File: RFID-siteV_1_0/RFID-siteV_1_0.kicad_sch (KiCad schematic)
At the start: 48 parts, among them J1 USB_C_Receptacle_USB2.0, J2 Conn_01x05_Male, J4 Conn_01x05_Female, Q1 MMBT3904, SW1 SW_Push, U1 XC6206P332MR, U2 STM32L053R8Tx

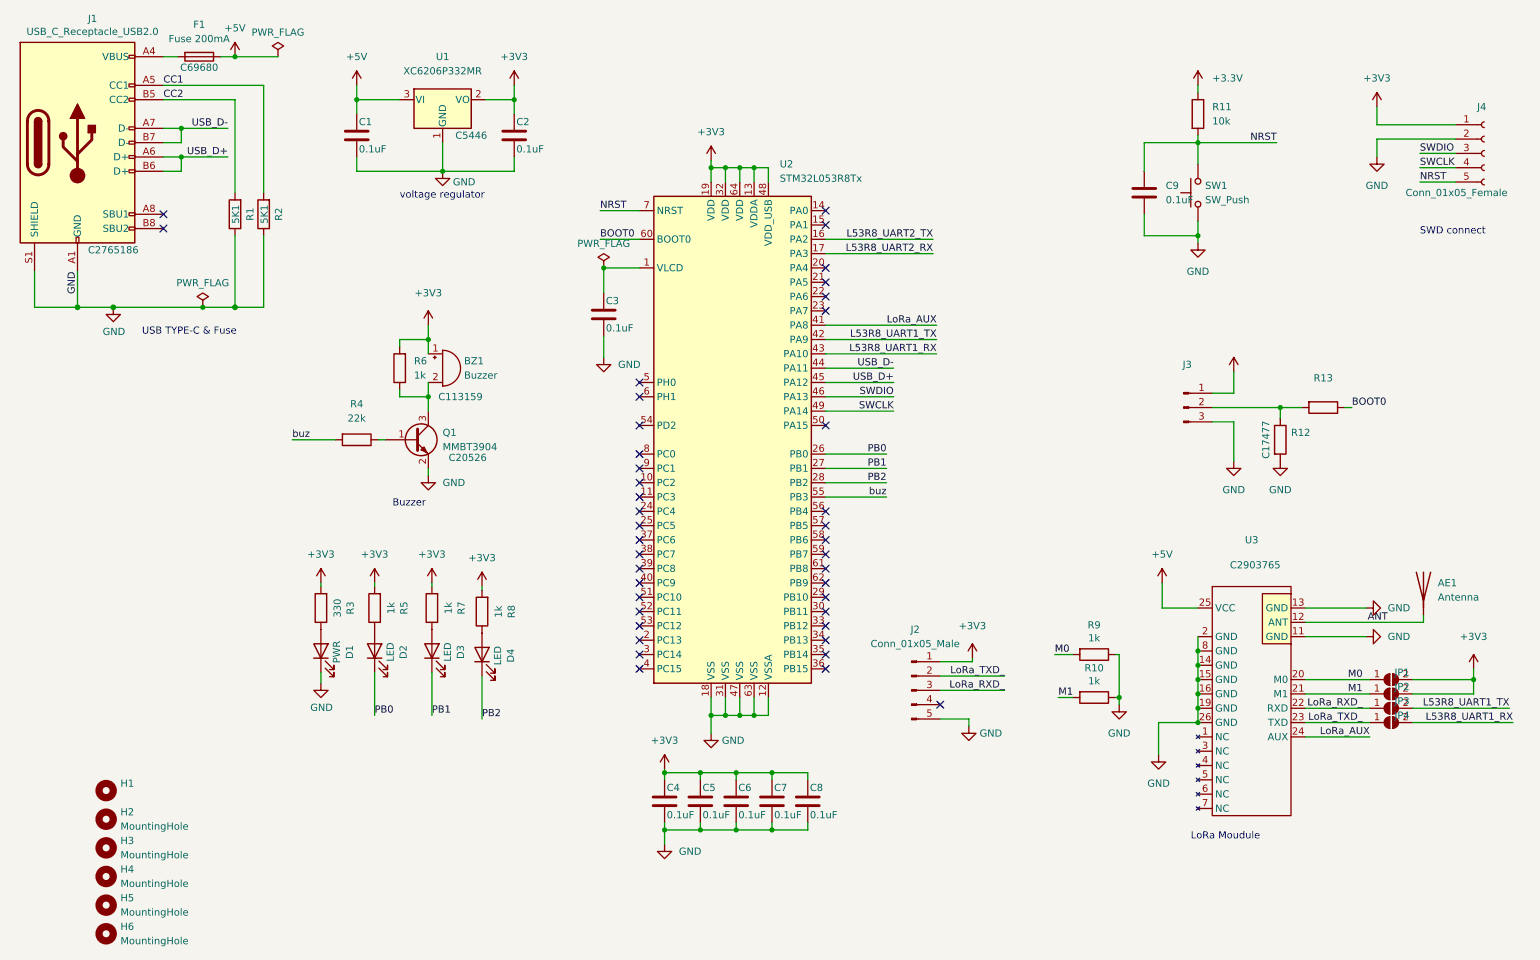
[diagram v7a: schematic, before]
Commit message: Update RFID-siteV_1_0.kicad_sch
add 模式選擇點(jump)
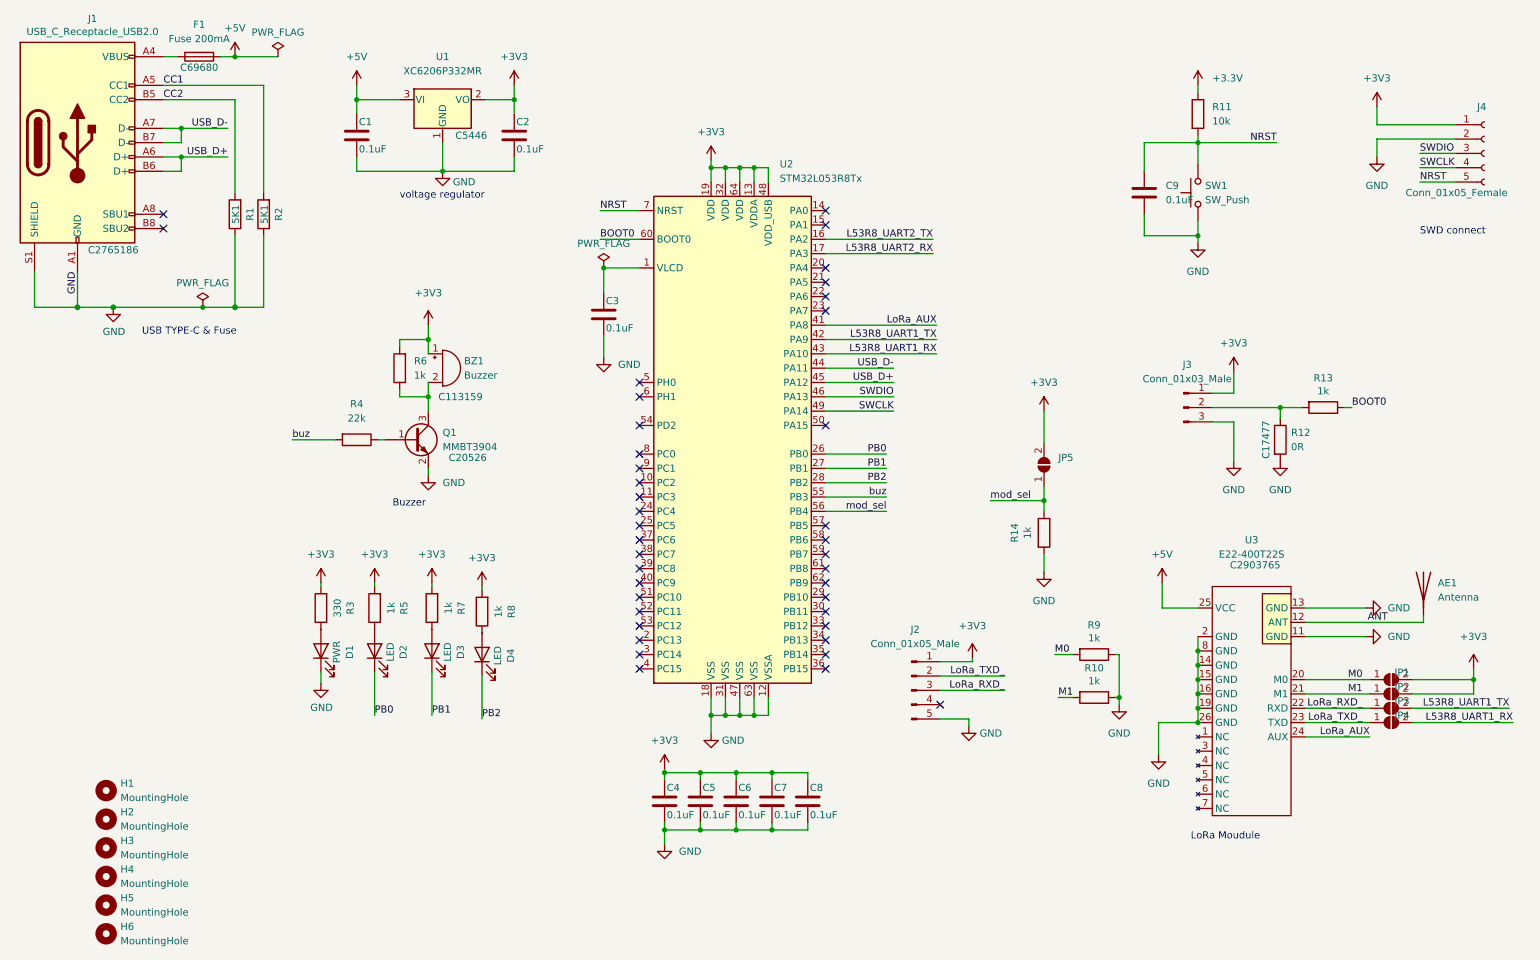
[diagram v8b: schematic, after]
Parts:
- added JP5: (no value), symbol Jumper:SolderJumper_2_Open
- added R14: 1k, Resistor_SMD:R_0805_2012Metric, symbol Device:R
- H1: value (none) -> MountingHole; footprint (none) -> MountingHole:MountingHole_2.5mm
- J3: value (none) -> Conn_01x03_Male; footprint (none) -> Connector_PinHeader_2.54mm:PinHeader_1x03_P2.54mm_Vertical
- R12: value (none) -> 0R; footprint (none) -> Resistor_SMD:R_0805_2012Metric
- R13: value (none) -> 1k; footprint (none) -> Resistor_SMD:R_0805_2012Metric
- U3: value (none) -> E22-400T22S
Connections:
- net +3V3: now also JP5.2 (B)
- net GND: now also R14.2
- net mod_sel: now reaches U2.56 (PB4)
- net mod_sel: now also JP5.1 (A), R14.1
- no-connect marks 41 -> 40
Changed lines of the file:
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@@
   (junction (at 151.13 148.59) (diameter 0) (color 0 0 0 0)
+  )
+  (junction (at 199.39 100.33) (diameter 0) (color 0 0 0 0)
   )
   (junction (at 226.695 53.34) (diameter 0) (color 0 0 0 0)
@@
   (no_connect (at 160.655 51.435))
   (no_connect (at 160.655 48.895))
-  (no_connect (at 160.655 102.235))
   (no_connect (at 160.655 66.675))
   (no_connect (at 160.655 64.135))
@@
     (stroke (width 0) (type default) (color 0 0 0 0))
   )
+  (wire (pts (xy 199.39 100.33) (xy 199.39 102.235))
+    (stroke (width 0) (type default) (color 0 0 0 0))
+  )
   (wire (pts (xy 140.335 138.43) (xy 142.875 138.43))
     (stroke (width 0) (type default) (color 0 0 0 0))
@@
     (stroke (width 0) (type default) (color 0 0 0 0))
   )
+  (wire (pts (xy 189.865 100.33) (xy 199.39 100.33))
+    (stroke (width 0) (type default) (color 0 0 0 0))
+  )
   (wire (pts (xy 226.695 132.08) (xy 226.695 134.62))
+    (stroke (width 0) (type default) (color 0 0 0 0))
+  )
+  (wire (pts (xy 199.39 97.79) (xy 199.39 100.33))
     (stroke (width 0) (type default) (color 0 0 0 0))
   )
@@
     (stroke (width 0) (type default) (color 0 0 0 0))
   )
+  (wire (pts (xy 160.655 102.235) (xy 171.45 102.235))
+    (stroke (width 0) (type default) (color 0 0 0 0))
+  )
   (wire (pts (xy 46.355 36.83) (xy 43.18 36.83))
     (stroke (width 0) (type default) (color 0 0 0 0))
@@
     (stroke (width 0) (type default) (color 0 0 0 0))
   )
+  (wire (pts (xy 199.39 109.855) (xy 199.39 113.03))
+    (stroke (width 0) (type default) (color 0 0 0 0))
+  )
   (wire (pts (xy 160.655 81.915) (xy 172.72 81.915))
     (stroke (width 0) (type default) (color 0 0 0 0))
@@
     (stroke (width 0) (type solid) (color 0 0 0 0))
   )
+  (wire (pts (xy 199.39 84.455) (xy 199.39 90.17))
+    (stroke (width 0) (type default) (color 0 0 0 0))
+  )
   (wire (pts (xy 50.165 66.04) (xy 55.88 66.04))
     (stroke (width 0) (type solid) (color 0 0 0 0))
@@
     (effects (font (size 1.27 1.27)) (justify right bottom))
   )
+  (label "mod_sel" (at 171.45 102.235 180)
+    (effects (font (size 1.27 1.27)) (justify right bottom))
+  )
   (label "SWCLK" (at 172.72 84.455 180)
     (effects (font (size 1.27 1.27)) (justify right bottom))
@@
   )
   (label "SWDIO" (at 266.065 38.735 0)
+    (effects (font (size 1.27 1.27)) (justify left bottom))
+  )
+  (label "mod_sel" (at 189.865 100.33 0)
     (effects (font (size 1.27 1.27)) (justify left bottom))
   )
@@
       (effects (font (size 1.27 1.27)) (justify left))
     )
-    (property "Value" "" (id 1) (at 243.205 90.8049 0)
-      (effects (font (size 1.27 1.27)) (justify left))
-    )
-    (property "Footprint" "" (id 2) (at 239.522 89.535 90)
+    (property "Value" "0R" (id 1) (at 243.205 90.8049 0)
+      (effects (font (size 1.27 1.27)) (justify left))
+    )
+    (property "Footprint" "Resistor_SMD:R_0805_2012Metric" (id 2) (at 239.522 89.535 90)
       (effects (font (size 1.27 1.27)) hide)
     )
@@
     (in_bom no) (on_board yes)
     (property "Reference" "U3" (id 0) (at 236.22 107.315 0))
-    (property "Value" "" (id 1) (at 236.22 109.855 0))
+    (property "Value" "E22-400T22S" (id 1) (at 236.22 109.855 0))
     (property "Footprint" "RF_Module:E220-400TxxS" (id 2) (at 236.22 112.395 0)
       (effects (font (size 1.27 1.27)) hide)
@@
       (effects (font (size 1.27 1.27)) (justify left))
     )
-    (property "Value" "" (id 1) (at 35.56 153.0349 0)
-      (effects (font (size 1.27 1.27)) (justify left))
-    )
-    (property "Footprint" "" (id 2) (at 33.02 151.765 0)
+    (property "Value" "MountingHole" (id 1) (at 35.56 153.0349 0)
+      (effects (font (size 1.27 1.27)) (justify left))
+    )
+    (property "Footprint" "MountingHole:MountingHole_2.5mm" (id 2) (at 33.02 151.765 0)
       (effects (font (size 1.27 1.27)) hide)
     )
@@
       (effects (font (size 1.27 1.27)) hide)
     )
+  )
+  (symbol (lib_id "Device:R") (at 199.39 106.045 0) (unit 1)
+    (in_bom yes) (on_board yes)
+    (property "Reference" "R14" (id 0) (at 194.1638 106.045 90))
+    (property "Value" "1k" (id 1) (at 196.463 106.045 90))
+    (property "Footprint" "Resistor_SMD:R_0805_2012Metric" (id 2) (at 197.612 106.045 90)
+      (effects (font (size 1.27 1.27)) hide)
+    )
+    (property "Datasheet" "~" (id 3) (at 199.39 106.045 0)
+      (effects (font (size 1.27 1.27)) hide)
+    )
+    (pin "1")
+    (pin "2")
   )
   (symbol (lib_id "Mechanical:MountingHole") (at 33.02 156.845 0) (unit 1)
@@
     (pin "1")
     (pin "2")
+  )
+  (symbol (lib_id "power:GND") (at 199.39 113.03 0) (unit 1)
+    (in_bom yes) (on_board yes) (fields_autoplaced)
+    (property "Reference" "#PWR034" (id 0) (at 199.39 119.38 0)
+      (effects (font (size 1.27 1.27)) hide)
+    )
+    (property "Value" "GND" (id 1) (at 199.39 118.11 0))
+    (property "Footprint" "" (id 2) (at 199.39 113.03 0)
+      (effects (font (size 1.27 1.27)) hide)
+    )
+    (property "Datasheet" "" (id 3) (at 199.39 113.03 0)
+      (effects (font (size 1.27 1.27)) hide)
+    )
+    (pin "1")
   )
   (symbol (lib_id "power:+3V3") (at 105.41 26.67 0) (unit 1)
@@
       (effects (font (size 1.27 1.27)) hide)
     )
-    (property "Value" "" (id 1) (at 233.045 72.39 0))
+    (property "Value" "+3V3" (id 1) (at 233.045 72.39 0))
     (property "Footprint" "" (id 2) (at 233.045 77.47 0)
       (effects (font (size 1.27 1.27)) hide)
@@
     (in_bom no) (on_board yes) (fields_autoplaced)
     (property "Reference" "J3" (id 0) (at 224.79 76.2 0))
-    (property "Value" "" (id 1) (at 224.79 78.74 0))
-    (property "Footprint" "" (id 2) (at 224.155 83.82 0)
+    (property "Value" "Conn_01x03_Male" (id 1) (at 224.79 78.74 0))
+    (property "Footprint" "Connector_PinHeader_2.54mm:PinHeader_1x03_P2.54mm_Vertical" (id 2) (at 224.155 83.82 0)
       (effects (font (size 1.27 1.27)) hide)
     )
@@
     (pin "1")
   )
+  (symbol (lib_id "Jumper:SolderJumper_2_Open") (at 199.39 93.98 90) (unit 1)
+    (in_bom yes) (on_board yes) (fields_autoplaced)
+    (property "Reference" "JP5" (id 0) (at 201.93 92.7099 90)
+      (effects (font (size 1.27 1.27)) (justify right))
+    )
+    (property "Value" "" (id 1) (at 201.93 95.2499 90)
+      (effects (font (size 1.27 1.27)) (justify right))
+    )
+    (property "Footprint" "" (id 2) (at 199.39 93.98 0)
+      (effects (font (size 1.27 1.27)) hide)
+    )
+    (property "Datasheet" "~" (id 3) (at 199.39 93.98 0)
+      (effects (font (size 1.27 1.27)) hide)
+    )
+    (pin "1")
+    (pin "2")
+  )
   (symbol (lib_id "Device:R") (at 248.92 83.82 270) (unit 1)
     (in_bom yes) (on_board yes)
     (property "Reference" "R13" (id 0) (at 248.92 78.5938 90))
-    (property "Value" "" (id 1) (at 248.92 80.893 90))
-    (property "Footprint" "" (id 2) (at 248.92 82.042 90)
+    (property "Value" "1k" (id 1) (at 248.92 80.893 90))
+    (property "Footprint" "Resistor_SMD:R_0805_2012Metric" (id 2) (at 248.92 82.042 90)
       (effects (font (size 1.27 1.27)) hide)
     )
@@
     (pin "1")
   )
+  (symbol (lib_id "power:+3V3") (at 199.39 84.455 0) (unit 1)
+    (in_bom yes) (on_board yes) (fields_autoplaced)
+    (property "Reference" "#PWR033" (id 0) (at 199.39 88.265 0)
+      (effects (font (size 1.27 1.27)) hide)
+    )
+    (property "Value" "+3V3" (id 1) (at 199.39 79.375 0))
+    (property "Footprint" "" (id 2) (at 199.39 84.455 0)
+      (effects (font (size 1.27 1.27)) hide)
+    )
+    (property "Datasheet" "" (id 3) (at 199.39 84.455 0)
+      (effects (font (size 1.27 1.27)) hide)
+    )
+    (pin "1")
+  )
   (symbol (lib_id "power:GND") (at 219.71 145.415 0) (unit 1)
     (in_bom yes) (on_board yes) (fields_autoplaced)
@@
       (reference "#PWR032") (unit 1) (value "+3V3") (footprint "")
     )
+    (path "/cd68be32-a6fe-4c8f-add6-4a5fecad271e"
+      (reference "#PWR033") (unit 1) (value "+3V3") (footprint "")
+    )
+    (path "/66067eaf-0d82-477a-a3f3-fd68b9e40cb0"
+      (reference "#PWR034") (unit 1) (value "GND") (footprint "")
+    )
     (path "/3ae1892a-0bb4-4f17-a391-4593a1c74cc5"
       (reference "AE1") (unit 1) (value "Antenna") (footprint "RF_Antenna:433MHz_V")
@@
       (reference "JP4") (unit 1) (value "SolderJumper_2_Open") (footprint "Jumper:SolderJumper-2_P1.3mm_Open_RoundedPad1.0x1.5mm")
     )
+    (path "/bee0e1c1-b842-441d-85d5-538540a63a14"
+      (reference "JP5") (unit 1) (value "SolderJumper_2_Open") (footprint "Jumper:SolderJumper-2_P1.3mm_Open_TrianglePad1.0x1.5mm")
+    )
     (path "/82f5ced0-6a77-4247-9e28-dff39ce9beef"
       (reference "Q1") (unit 1) (value "MMBT3904") (footprint "Package_TO_SOT_SMD:SOT-23")
@@
       (reference "R13") (unit 1) (value "1k") (footprint "Resistor_SMD:R_0805_2012Metric")
     )
+    (path "/48498ce7-eca9-44e0-bc6d-7ca5752498ba"
+      (reference "R14") (unit 1) (value "1k") (footprint "Resistor_SMD:R_0805_2012Metric")
+    )
     (path "/fdd48cbc-c4f6-4e8d-b774-1cd02a92d89d"
